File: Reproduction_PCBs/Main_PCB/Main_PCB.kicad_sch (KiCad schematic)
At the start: 5 parts

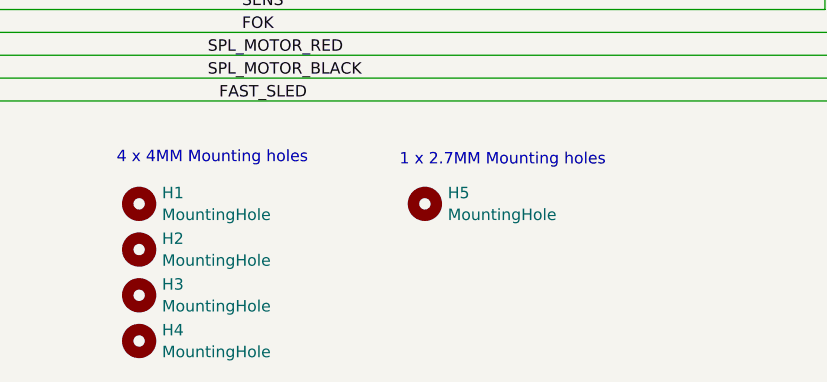
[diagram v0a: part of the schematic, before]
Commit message: Final fixes to include some ectra mounting holes + GND connection to shield
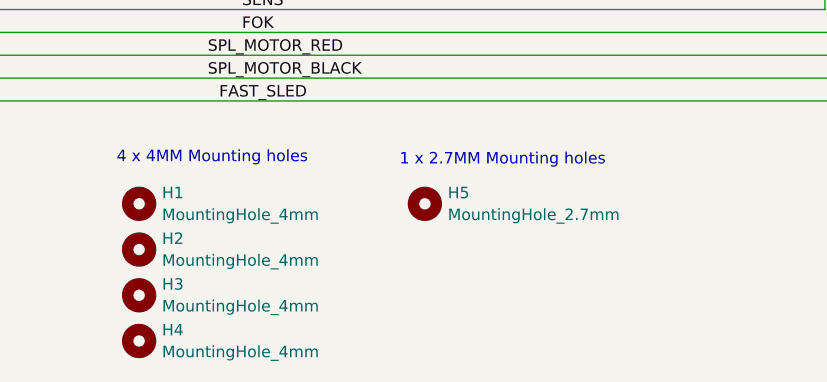
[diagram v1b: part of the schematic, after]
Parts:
- H1, H2, H3, H4: value MountingHole -> MountingHole_4mm; footprint MountingHole:MountingHole_4mm -> PC-Engine_CDR-30A:MountingHole_4mm; symbol Mechanical:MountingHole -> PC-Engine_CDR-30:MountingHole_4mm
- H5: value MountingHole -> MountingHole_2.7mm; footprint MountingHole:MountingHole_2.7mm -> PC-Engine_CDR-30A:MountingHole_2.7mm; symbol Mechanical:MountingHole -> PC-Engine_CDR-30:MountingHole_2.7mm
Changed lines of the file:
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@@
 	(title_block
 		(title "PC-Engine CDR-30A (CD-ROM2) MAIN PWR Reproduction")
-		(date "2025-02-23")
+		(date "2025-02-24")
 		(rev "0.1")
 		(company "Author: Regis Galland")
@@
 	)
 	(symbol
-		(lib_id "Mechanical:MountingHole")
+		(lib_id "PC-Engine_CDR-30:MountingHole_4mm")
 		(at 88.9 177.8 0)
 		(unit 1)
@@
 			)
 		)
-		(property "Value" "MountingHole"
+		(property "Value" "MountingHole_4mm"
 			(at 91.44 179.0121 0)
 			(effects
@@
 			)
 		)
-		(property "Footprint" "MountingHole:MountingHole_4mm"
+		(property "Footprint" "PC-Engine_CDR-30A:MountingHole_4mm"
 			(at 88.9 177.8 0)
 			(effects
@@
 	)
 	(symbol
-		(lib_id "Mechanical:MountingHole")
+		(lib_id "PC-Engine_CDR-30:MountingHole_4mm")
 		(at 88.9 187.96 0)
 		(unit 1)
@@
 			)
 		)
-		(property "Value" "MountingHole"
+		(property "Value" "MountingHole_4mm"
 			(at 91.44 189.1721 0)
 			(effects
@@
 			)
 		)
-		(property "Footprint" "MountingHole:MountingHole_4mm"
+		(property "Footprint" "PC-Engine_CDR-30A:MountingHole_4mm"
 			(at 88.9 187.96 0)
 			(effects
@@
 	)
 	(symbol
-		(lib_id "Mechanical:MountingHole")
+		(lib_id "PC-Engine_CDR-30:MountingHole_4mm")
 		(at 88.9 182.88 0)
 		(unit 1)
@@
 			)
 		)
-		(property "Value" "MountingHole"
+		(property "Value" "MountingHole_4mm"
 			(at 91.44 184.0921 0)
 			(effects
@@
 			)
 		)
-		(property "Footprint" "MountingHole:MountingHole_4mm"
+		(property "Footprint" "PC-Engine_CDR-30A:MountingHole_4mm"
 			(at 88.9 182.88 0)
 			(effects
@@
 	)
 	(symbol
-		(lib_id "Mechanical:MountingHole")
+		(lib_id "PC-Engine_CDR-30:MountingHole_4mm")
 		(at 88.9 193.04 0)
 		(unit 1)
@@
 			)
 		)
-		(property "Value" "MountingHole"
+		(property "Value" "MountingHole_4mm"
 			(at 91.44 194.2521 0)
 			(effects
@@
 			)
 		)
-		(property "Footprint" "MountingHole:MountingHole_4mm"
+		(property "Footprint" "PC-Engine_CDR-30A:MountingHole_4mm"
 			(at 88.9 193.04 0)
 			(effects
@@
 	)
 	(symbol
-		(lib_id "Mechanical:MountingHole")
+		(lib_id "PC-Engine_CDR-30:MountingHole_2.7mm")
 		(at 120.65 177.8 0)
 		(unit 1)
@@
 			)
 		)
-		(property "Value" "MountingHole"
+		(property "Value" "MountingHole_2.7mm"
 			(at 123.19 179.0121 0)
 			(effects
@@
 			)
 		)
-		(property "Footprint" "MountingHole:MountingHole_2.7mm"
+		(property "Footprint" "PC-Engine_CDR-30A:MountingHole_2.7mm"
 			(at 120.65 177.8 0)
 			(effects
